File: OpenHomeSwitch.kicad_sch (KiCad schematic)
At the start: 12 parts, among them J3 Debug, J3 Extension I2C, J3 Extension UART, U6 SRV05-4

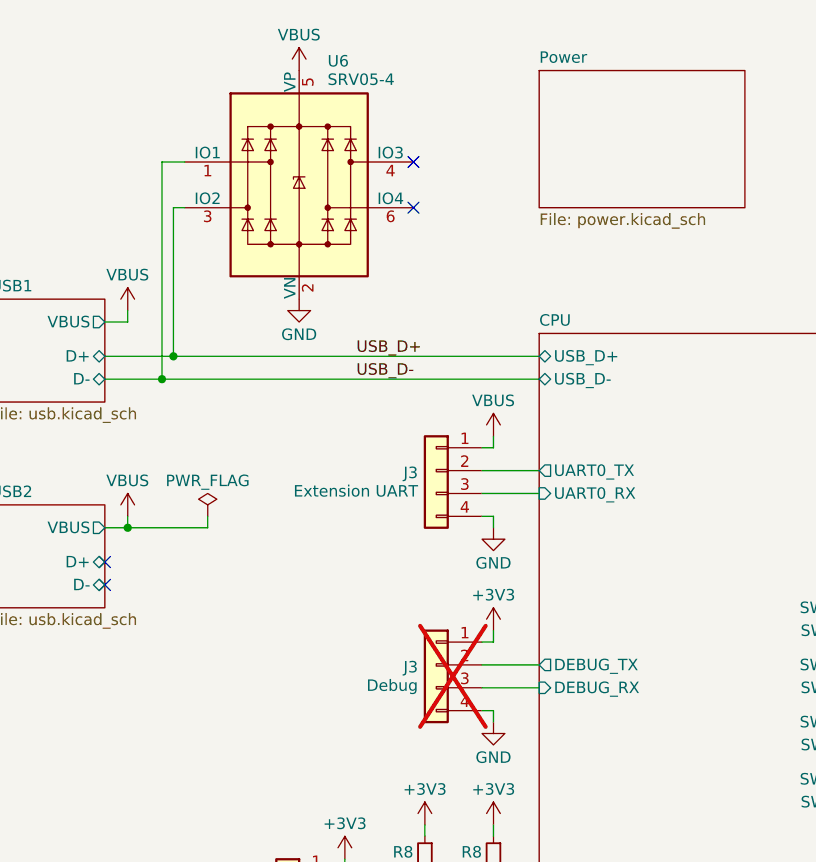
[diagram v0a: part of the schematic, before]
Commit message: Finish routing for the most part
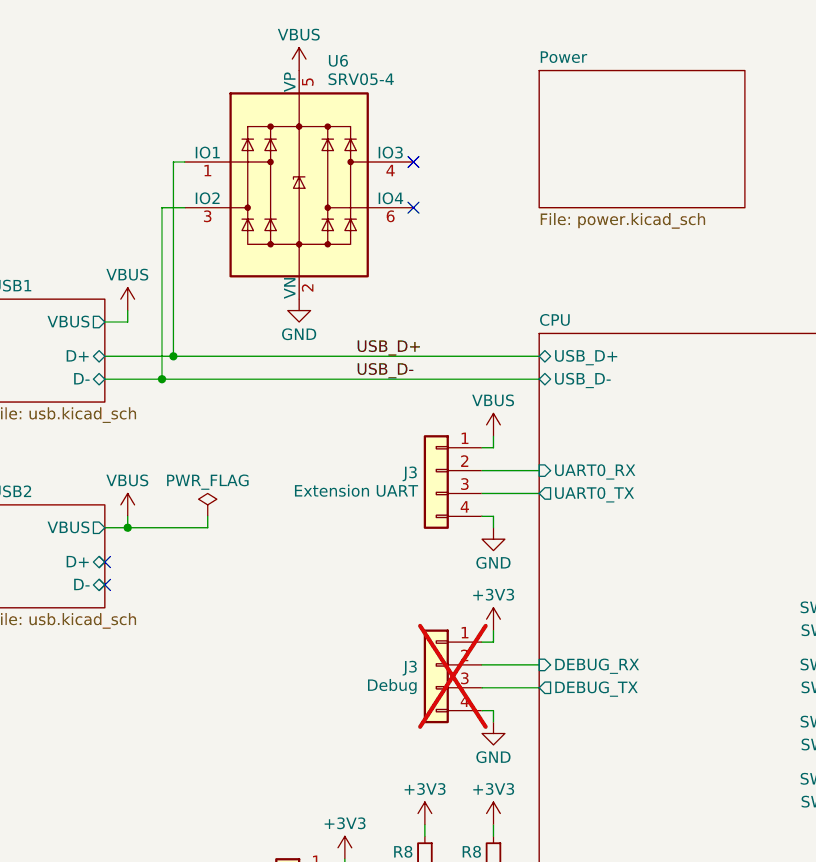
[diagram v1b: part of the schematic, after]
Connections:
- net CPU/DEBUG_RX: now also J3.2 (Pin_2); no longer J3.3 (Pin_3)
- net CPU/DEBUG_TX: now also J3.3 (Pin_3); no longer J3.2 (Pin_2)
- net CPU/UART0_RX: now also J3.2 (Pin_2); no longer J3.3 (Pin_3)
- net CPU/UART0_TX: now also J3.3 (Pin_3); no longer J3.2 (Pin_2)
- net USB_D+: now also U6.1 (IO1); no longer U6.3 (IO2)
- net USB_D-: now also U6.3 (IO2); no longer U6.1 (IO1)
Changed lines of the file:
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@@
-    (stroke (width 0) (type default))
-  )
-  (wire (pts (xy 72.39 62.23) (xy 71.12 62.23))
     (stroke (width 0) (type default))
   )
@@
     (stroke (width 0) (type default))
   )
+  (wire (pts (xy 71.12 57.15) (xy 72.39 57.15))
+    (stroke (width 0) (type default))
+  )
   (wire (pts (xy 30.48 22.86) (xy 30.48 24.13))
     (stroke (width 0) (type default))
@@
     (stroke (width 0) (type default))
   )
+  (wire (pts (xy 69.85 62.23) (xy 69.85 81.28))
+    (stroke (width 0) (type default))
+  )
   (wire (pts (xy 106.68 119.38) (xy 106.68 118.11))
     (stroke (width 0) (type default))
@@
     (stroke (width 0) (type default))
   )
-  (wire (pts (xy 69.85 57.15) (xy 69.85 81.28))
-    (stroke (width 0) (type default))
-  )
   (wire (pts (xy 99.06 140.97) (xy 111.76 140.97))
     (stroke (width 0) (type default))
@@
     (stroke (width 0) (type default))
   )
-  (wire (pts (xy 69.85 57.15) (xy 72.39 57.15))
-    (stroke (width 0) (type default))
-  )
   (wire (pts (xy 66.04 73.66) (xy 66.04 74.93))
     (stroke (width 0) (type default))
@@
     (stroke (width 0) (type default))
   )
+  (wire (pts (xy 69.85 62.23) (xy 72.39 62.23))
+    (stroke (width 0) (type default))
+  )
   (wire (pts (xy 66.04 97.79) (xy 63.5 97.79))
     (stroke (width 0) (type default))
@@
     (stroke (width 0) (type default))
   )
-  (wire (pts (xy 71.12 62.23) (xy 71.12 78.74))
+  (wire (pts (xy 71.12 57.15) (xy 71.12 78.74))
     (stroke (width 0) (type default))
   )
@@
       (effects (font (size 1.27 1.27)) (justify right))
     )
-    (pin "DEBUG_TX" output (at 111.76 113.03 180)
-      (effects (font (size 1.27 1.27)) (justify left))
-    )
-    (pin "DEBUG_RX" input (at 111.76 115.57 180)
-      (effects (font (size 1.27 1.27)) (justify left))
-    )
-    (pin "UART0_TX" output (at 111.76 91.44 180)
-      (effects (font (size 1.27 1.27)) (justify left))
-    )
-    (pin "UART0_RX" input (at 111.76 93.98 180)
-      (effects (font (size 1.27 1.27)) (justify left))
-    )
+    (pin "DEBUG_TX" output (at 111.76 115.57 180)
+      (effects (font (size 1.27 1.27)) (justify left))
+    )
+    (pin "DEBUG_RX" input (at 111.76 113.03 180)
+      (effects (font (size 1.27 1.27)) (justify left))
+    )
+    (pin "UART0_TX" output (at 111.76 93.98 180)
+      (effects (font (size 1.27 1.27)) (justify left))
+    )
+    (pin "UART0_RX" input (at 111.76 91.44 180)
+      (effects (font (size 1.27 1.27)) (justify left))
+    )

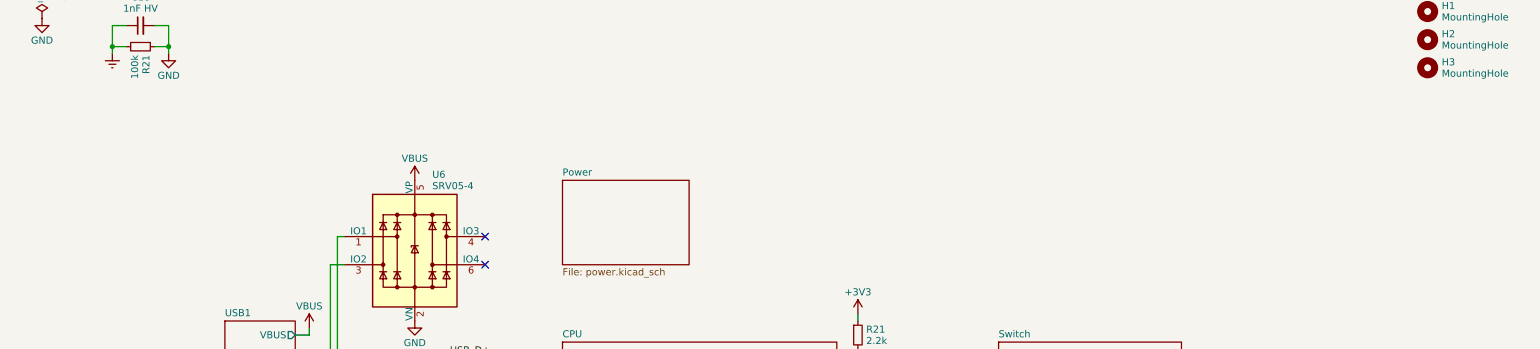
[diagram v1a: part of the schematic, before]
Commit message: Finalize design
- Layout last signals
- Hide designators
- Add more LEDs
- Add tooling holes
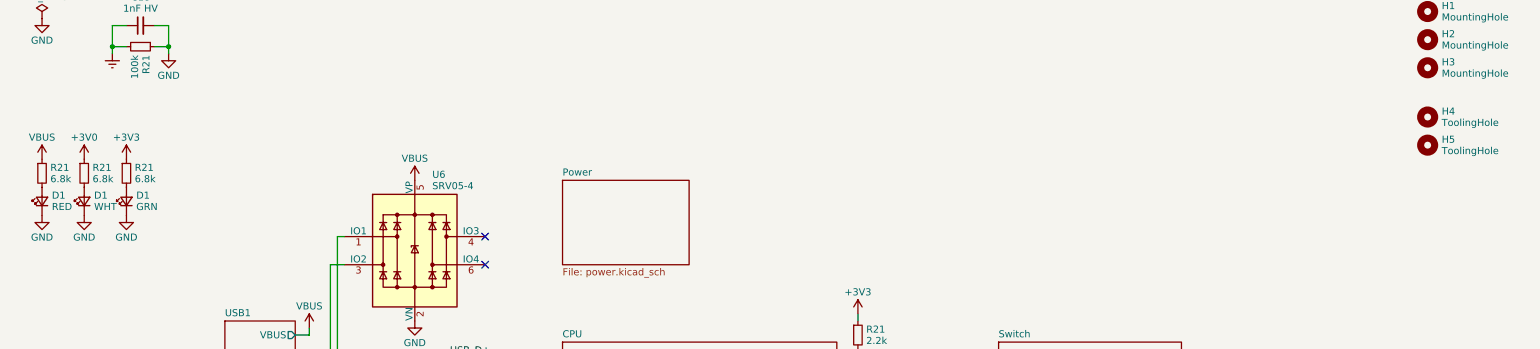
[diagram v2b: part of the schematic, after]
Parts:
- added D1: GRN, LED_SMD:LED_0603_1608Metric, symbol Device:LED_Small
- added D1: RED, LED_SMD:LED_0603_1608Metric, symbol Device:LED_Small
- added D1: WHT, LED_SMD:LED_0603_1608Metric, symbol Device:LED_Small
- added H4, H5: ToolingHole, ToolingHole:ToolingHole_JLCSMT, symbol Mechanical:MountingHole
- added R21 (x3): 6.8k, Resistor_SMD:R_0402_1005Metric, symbol Device:R_Small
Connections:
- net +3V3: now also R21.1
- net GND: now also D1.1 (K), D1.1 (K), D1.1 (K)
- net VBUS: now also R21.1
- new net: D1.2 (A), R21.2 (x3)
- new net +3V0: R21.1

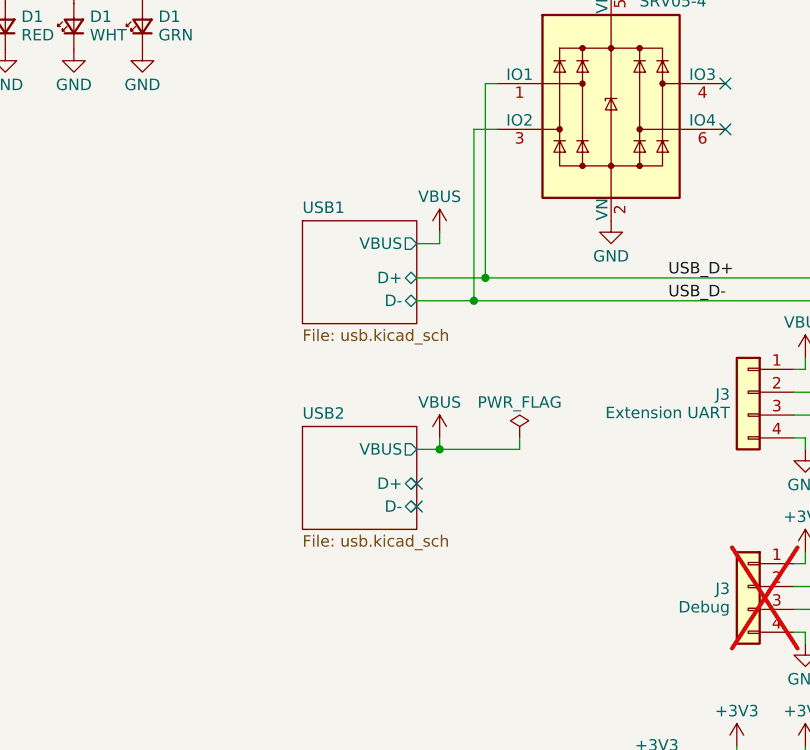
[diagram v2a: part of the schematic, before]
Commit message: Connect shield net to second USB port
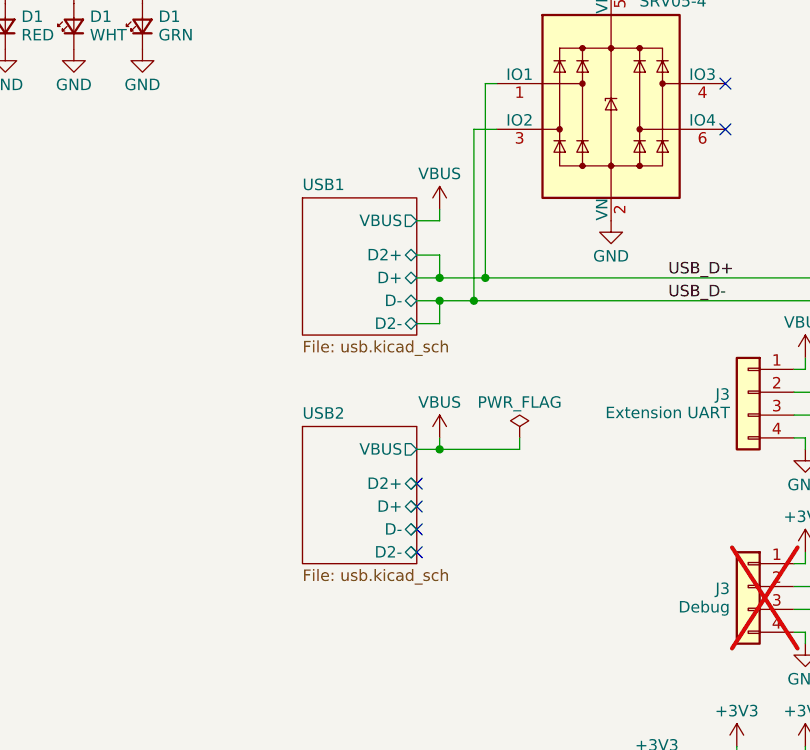
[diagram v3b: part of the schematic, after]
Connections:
- no-connect marks 4 -> 6
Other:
- sheet USB1 ports: added D2+, D2-; removed none
- sheet USB2 ports: added D2+, D2-; removed none
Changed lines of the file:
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@@
   (junction (at 106.68 138.43) (diameter 0) (color 0 0 0 0)
   )
+  (junction (at 66.04 81.28) (diameter 0) (color 0 0 0 0)
+  )
+  (junction (at 66.04 78.74) (diameter 0) (color 0 0 0 0)
+  )
   (junction (at 99.06 140.97) (diameter 0) (color 0 0 0 0)
   )
+  (no_connect (at 63.5 106.68))
+  (no_connect (at 63.5 109.22))
   (no_connect (at 97.79 62.23))
   (no_connect (at 97.79 57.15))
@@
     (stroke (width 0) (type default))
   )
+  (wire (pts (xy 63.5 76.2) (xy 66.04 76.2))
+    (stroke (width 0) (type default))
+  )
   (wire (pts (xy 161.29 128.27) (xy 190.5 128.27))
     (stroke (width 0) (type default))
   )
+  (wire (pts (xy 66.04 78.74) (xy 71.12 78.74))
+    (stroke (width 0) (type default))
+  )
   (wire (pts (xy 105.41 91.44) (xy 111.76 91.44))
     (stroke (width 0) (type default))
@@
     (stroke (width 0) (type default))
   )
-  (wire (pts (xy 66.04 74.93) (xy 63.5 74.93))
+  (wire (pts (xy 66.04 72.39) (xy 63.5 72.39))
     (stroke (width 0) (type default))
   )
@@
     (stroke (width 0) (type default))
   )
-  (wire (pts (xy 66.04 73.66) (xy 66.04 74.93))
+  (wire (pts (xy 66.04 81.28) (xy 69.85 81.28))
+    (stroke (width 0) (type default))
+  )
+  (wire (pts (xy 66.04 71.12) (xy 66.04 72.39))
     (stroke (width 0) (type default))
   )
@@
     (stroke (width 0) (type default))
   )
+  (wire (pts (xy 66.04 76.2) (xy 66.04 78.74))
+    (stroke (width 0) (type default))
+  )
   (wire (pts (xy 161.29 106.68) (xy 190.5 106.68))
     (stroke (width 0) (type default))
@@
     (stroke (width 0) (type default))
   )
-  (wire (pts (xy 63.5 78.74) (xy 71.12 78.74))
+  (wire (pts (xy 63.5 78.74) (xy 66.04 78.74))
     (stroke (width 0) (type default))
   )
@@
     (stroke (width 0) (type default))
   )
+  (wire (pts (xy 66.04 83.82) (xy 66.04 81.28))
+    (stroke (width 0) (type default))
+  )
+  (wire (pts (xy 63.5 83.82) (xy 66.04 83.82))
+    (stroke (width 0) (type default))
+  )
   (wire (pts (xy 161.29 78.74) (xy 190.5 78.74))
     (stroke (width 0) (type default))
@@
     (stroke (width 0) (type default))
   )
-  (wire (pts (xy 63.5 81.28) (xy 69.85 81.28))
+  (wire (pts (xy 63.5 81.28) (xy 66.04 81.28))
     (stroke (width 0) (type default))
   )
@@
     )
   )
-  (symbol (lib_id "power:VBUS") (at 66.04 73.66 0) (unit 1)
-    (in_bom yes) (on_board yes) (dnp no) (fields_autoplaced)
-    (property "Reference" "#PWR0151" (at 66.04 77.47 0)
-      (effects (font (size 1.27 1.27)) hide)
-    )
-    (property "Value" "VBUS" (at 66.04 69.715 0)
-      (effects (font (size 1.27 1.27)))
-    )
-    (property "Footprint" "" (at 66.04 73.66 0)
-      (effects (font (size 1.27 1.27)) hide)
-    )
-    (property "Datasheet" "" (at 66.04 73.66 0)
+  (symbol (lib_id "power:VBUS") (at 66.04 71.12 0) (unit 1)
+    (in_bom yes) (on_board yes) (dnp no) (fields_autoplaced)
+    (property "Reference" "#PWR0151" (at 66.04 74.93 0)
+      (effects (font (size 1.27 1.27)) hide)
+    )
+    (property "Value" "VBUS" (at 66.04 67.175 0)
+      (effects (font (size 1.27 1.27)))
+    )
+    (property "Footprint" "" (at 66.04 71.12 0)
+      (effects (font (size 1.27 1.27)) hide)
+    )
+    (property "Datasheet" "" (at 66.04 71.12 0)
       (effects (font (size 1.27 1.27)) hide)
     )
@@
     )
   )
-  (sheet (at 50.8 72.39) (size 12.7 11.43) (fields_autoplaced)
+  (sheet (at 50.8 69.85) (size 12.7 15.24) (fields_autoplaced)
     (stroke (width 0.1524) (type solid))
     (fill (color 0 0 0 0.0000))
-    (property "Sheetname" "USB1" (at 50.8 71.6784 0)
+    (property "Sheetname" "USB1" (at 50.8 69.1384 0)
       (effects (font (size 1.27 1.27)) (justify left bottom))
     )
-    (property "Sheetfile" "usb.kicad_sch" (at 50.8 84.4046 0)
+    (property "Sheetfile" "usb.kicad_sch" (at 50.8 85.6746 0)
       (effects (font (size 1.27 1.27)) (justify left top))
     )
@@
       (effects (font (size 1.27 1.27)) (justify right))
     )
-    (pin "VBUS" output (at 63.5 74.93 0)
+    (pin "VBUS" output (at 63.5 72.39 0)
+      (effects (font (size 1.27 1.27)) (justify right))
+    )
+    (pin "D2-" bidirectional (at 63.5 83.82 0)
+      (effects (font (size 1.27 1.27)) (justify right))
+    )
+    (pin "D2+" bidirectional (at 63.5 76.2 0)
       (effects (font (size 1.27 1.27)) (justify right))
     )
@@
     )
   )
-  (sheet (at 50.8 95.25) (size 12.7 11.43) (fields_autoplaced)
+  (sheet (at 50.8 95.25) (size 12.7 15.24) (fields_autoplaced)
     (stroke (width 0.1524) (type solid))
     (fill (color 0 0 0 0.0000))
@@
       (effects (font (size 1.27 1.27)) (justify left bottom))
     )
-    (property "Sheetfile" "usb.kicad_sch" (at 50.8 107.2646 0)
+    (property "Sheetfile" "usb.kicad_sch" (at 50.8 111.0746 0)
       (effects (font (size 1.27 1.27)) (justify left top))
     )
-    (pin "D+" bidirectional (at 63.5 101.6 0)
-      (effects (font (size 1.27 1.27)) (justify right))
-    )
-    (pin "D-" bidirectional (at 63.5 104.14 0)
+    (pin "D+" bidirectional (at 63.5 104.14 0)
+      (effects (font (size 1.27 1.27)) (justify right))
+    )
+    (pin "D-" bidirectional (at 63.5 106.68 0)
       (effects (font (size 1.27 1.27)) (justify right))
     )
@@
       (effects (font (size 1.27 1.27)) (justify right))
     )
+    (pin "D2-" bidirectional (at 63.5 109.22 0)
+      (effects (font (size 1.27 1.27)) (justify right))
+    )
+    (pin "D2+" bidirectional (at 63.5 101.6 0)
+      (effects (font (size 1.27 1.27)) (justify right))
+    )

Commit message: Fix LCSC part numbers
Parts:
- J3: LCSC C780062 -> C5346656; now left out of the parts list
- J3: LCSC C780062 -> C5346656
- U6: LCSC (none) -> C85364
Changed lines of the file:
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@@
   )
   (symbol (lib_id "Connector_Generic:Conn_01x04") (at 100.33 113.03 0) (mirror y) (unit 1)
-    (in_bom yes) (on_board yes) (dnp yes)
+    (in_bom no) (on_board yes) (dnp yes)
     (property "Reference" "J3" (at 98.298 113.276 0)
       (effects (font (size 1.27 1.27)) (justify left))
@@
       (effects (font (size 1.27 1.27)) hide)
     )
-    (property "LCSC" "C780062" (at 100.33 113.03 90)
+    (property "LCSC" "C5346656" (at 100.33 113.03 90)
       (effects (font (size 1.27 1.27)) hide)
     )
@@
       (effects (font (size 1.27 1.27)) hide)
     )
-    (property "LCSC" "C780062" (at 100.33 91.44 90)
+    (property "LCSC" "C5346656" (at 100.33 91.44 90)
       (effects (font (size 1.27 1.27)) hide)
     )
@@
     )
     (property "Datasheet" "http://www.onsemi.com/pub/Collateral/SRV05-4-D.PDF" (at 85.09 59.69 0)
+      (effects (font (size 1.27 1.27)) hide)
+    )
+    (property "LCSC" "C85364" (at 85.09 59.69 0)
       (effects (font (size 1.27 1.27)) hide)
     )
@@
       (effects (font (size 1.27 1.27)) hide)
     )
-    (property "LCSC" "C780062" (at 83.82 138.43 90)
-      (effects (font (size 1.27 1.27)) hide)
-    )
+    (property "LCSC" "C5346656" (at 83.82 138.43 90)
+      (effects (font (size 1.27 1.27)) hide)
+    )

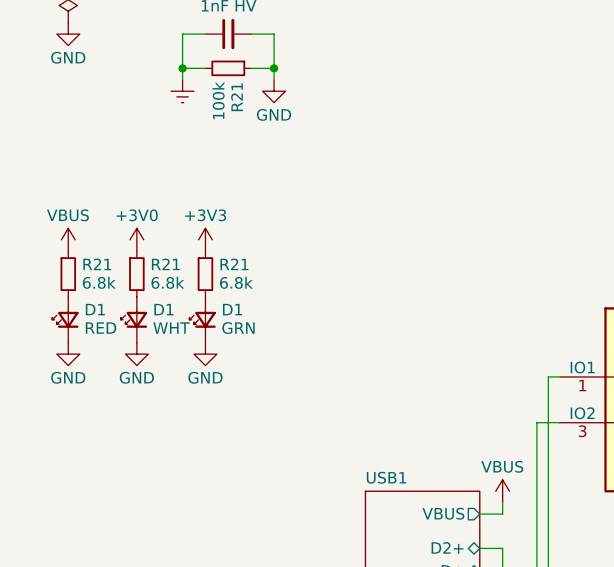
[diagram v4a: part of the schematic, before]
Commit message: Replace LED current limiting resistors to equalize brightness
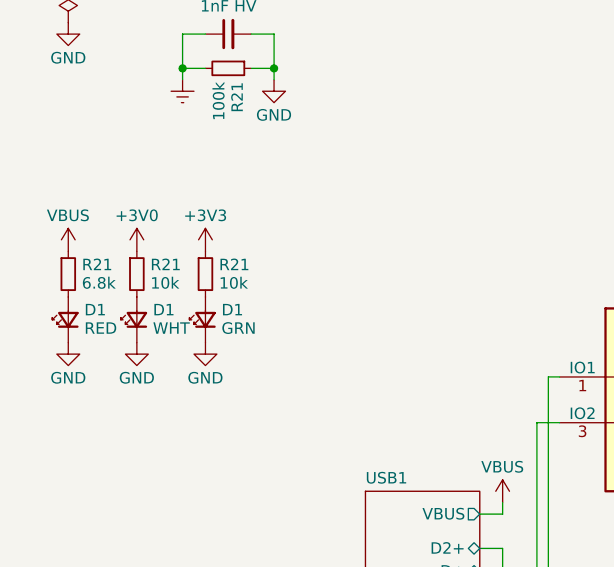
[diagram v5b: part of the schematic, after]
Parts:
- R21: value 6.8k -> 10k; LCSC C25917 -> C25744
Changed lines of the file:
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@@
       (effects (font (size 1.27 1.27)) (justify left))
     )
-    (property "Value" "6.8k" (at 34.5186 46.744 0)
+    (property "Value" "10k" (at 34.5186 46.744 0)
       (effects (font (size 1.27 1.27)) (justify left))
     )
@@
       (effects (font (size 1.27 1.27)) hide)
     )
-    (property "LCSC" "C25917" (at 33.02 45.72 0)
+    (property "LCSC" "C25744" (at 33.02 45.72 0)
       (effects (font (size 1.27 1.27)) hide)
     )
@@
       (effects (font (size 1.27 1.27)) (justify left))
     )
-    (property "Value" "6.8k" (at 26.8986 46.744 0)
+    (property "Value" "10k" (at 26.8986 46.744 0)
       (effects (font (size 1.27 1.27)) (justify left))
     )
@@
       (effects (font (size 1.27 1.27)) hide)
     )
-    (property "LCSC" "C25917" (at 25.4 45.72 0)
-      (effects (font (size 1.27 1.27)) hide)
-    )
+    (property "LCSC" "C25744" (at 25.4 45.72 0)
+      (effects (font (size 1.27 1.27)) hide)
+    )
